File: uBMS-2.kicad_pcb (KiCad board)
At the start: 4 copper layers, 60 x 90 mm, 183 parts, among them J1 Conn_02x03_Counter_Clockwise, J2 Conn_01x02, J3 Conn_01x01, J4 Conn_01x01, J5 Conn_02x07_Odd_Even, J6 Conn_02x07_Odd_Even, J7 Conn_02x07_Odd_Even, J8 Conn_01x01, Q1 2N7002, Q10 FQD5N20L, Q11 FQD5N20L, Q12 FQD5N20L, Q13 FQD5N20L, Q14 FQD5N20L, Q15 FQD5N20L, Q2 2N7002, Q3 NTD5865NL, Q4 FQD5N20L, Q5 FQD5N20L, Q6 FQD5N20L, Q7 FQD5N20L, Q8 FQD5N20L, Q9 FQD5N20L, U1 LM2576HVS-5, U10 CD74HC4067SM, U11 CD74HC4067SM, U2 ADS1115IDGS, U3 TLV1117-33, U4 TL431DBZ, U5 ESP32-WROOM-32, U6 TSC2012IDT, U7 MCP23017_SS, U8 MCP23008-E_P, U9 VDMG10C0

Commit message: Everything is finally routed
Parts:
- moved D3 0.81 mm to (47.4, 87.7)
- moved R4 0.81 mm to (47.4, 86.2)
- moved TH2 0.43 mm to (53.3, 76.8)
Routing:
- net GND: track 104.2 -> 198.8 mm, vias 11 -> 39
- net /TempMultiplex/ESP_Temp: track 0.00 -> 92.7 mm, vias 0 -> 2
- net /TempMultiplex/Mosfet_Temp: track 12.5 -> 104.8 mm, vias 1 -> 5
- net /TempMultiplex/Power_Temp: track 0.00 -> 83.7 mm, vias 0 -> 3
- net /S2_V: track 0.00 -> 82.0 mm, vias 0 -> 2
- net /S3_V: track 0.00 -> 81.1 mm, vias 0 -> 2
- net /PrgmNode: track 0.00 -> 81.1 mm, vias 0 -> 5
- net /BTN_2: track 10.5 -> 88.0 mm, vias 1 -> 3
- net +3V3: track 163.0 -> 237.8 mm, vias 6 -> 13
- net +5V: track 76.3 -> 144.7 mm, vias 6 -> 10
- net /BTN_1: track 6.19 -> 65.1 mm, vias 1 -> 3
- net /EN: track 8.77 -> 57.0 mm, vias 0 -> 1
- net /GPIO0: track 6.69 -> 48.7 mm, vias 0 -> 3
- net /TempMultiplex/Balance_Temp: track 0.00 -> 26.4 mm, vias 0 -> 4
- net Net-(D2-Pad1): track 5.71 -> 29.5 mm, vias 0 -> 4
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- added copper zone on In2.Cu, net +5V
- added copper zone on B.Cu, net GND
- added copper zone on In1.Cu, net GND

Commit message: Fixed connections
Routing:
- net +5V: track 144.7 -> 166.4 mm, vias 10 -> 15
- net GND: track 198.8 -> 219.0 mm
- net Net-(Q3-Pad1): track 0.00 -> 2.94 mm, vias 0 -> 1
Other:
- rule trace_min: 0.2 -> 0.09
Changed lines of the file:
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@@
     (thickness 1.6)
     (drawings 8)
-    (tracks 1995)
+    (tracks 2030)
     (zones 0)
     (modules 183)
@@
   )
   (setup
-    (last_trace_width 0.2)
+    (last_trace_width 0.25)
     (user_trace_width 0.2)
     (user_trace_width 0.5)
@@
     (zone_clearance 0.508)
     (zone_45_only no)
-    (trace_min 0.2)
+    (trace_min 0.09)
     (via_size 0.8)
     (via_drill 0.4)
@@
   (via (at 75.75 56.5) (size 0.8) (drill 0.4) (layers F.Cu B.Cu) (net 1))
   (via (at 74.75 56.5) (size 0.8) (drill 0.4) (layers F.Cu B.Cu) (net 1))
-  (via (at 77.75 56.5) (size 0.8) (drill 0.4) (layers F.Cu B.Cu) (net 1))
-  (via (at 78.75 56.5) (size 0.8) (drill 0.4) (layers F.Cu B.Cu) (net 1))
+  (segment (start 27.1 36.9) (end 27.2 36.8) (width 0.5) (layer B.Cu) (net 1))
+  (segment (start 27.1 39.025) (end 27.1 36.9) (width 0.5) (layer B.Cu) (net 1))
+  (segment (start 27.2 34.55) (end 27.55 34.2) (width 0.5) (layer B.Cu) (net 1))
+  (segment (start 27.2 36.8) (end 27.2 34.55) (width 0.5) (layer B.Cu) (net 1))
+  (via (at 28.5 36.75) (size 0.8) (drill 0.4) (layers F.Cu B.Cu) (net 1))
+  (segment (start 27.2 36.8) (end 28.45 36.8) (width 0.5) (layer B.Cu) (net 1))
+  (segment (start 28.45 36.8) (end 28.5 36.75) (width 0.5) (layer B.Cu) (net 1))
+  (segment (start 40.234315 60.2) (end 40.8 60.2) (width 0.5) (layer B.Cu) (net 1))
+  (segment (start 36 60.2) (end 40.234315 60.2) (width 0.5) (layer B.Cu) (net 1))
+  (segment (start 34.375 61.825) (end 36 60.2) (width 0.5) (layer B.Cu) (net 1))
+  (segment (start 33.65 61.825) (end 34.375 61.825) (width 0.5) (layer B.Cu) (net 1))
+  (segment (start 23.6 66.8) (end 23.849999 66.8) (width 0.5) (layer F.Cu) (net 1))
+  (via (at 27.75 63.25) (size 0.8) (drill 0.4) (layers F.Cu B.Cu) (net 1))
+  (segment (start 27.75 63.525) (end 27.75 63.25) (width 0.5) (layer F.Cu) (net 1))
+  (segment (start 23.6 66.8) (end 24.475 66.8) (width 0.5) (layer F.Cu) (net 1))
+  (segment (start 24.475 66.8) (end 27.75 63.525) (width 0.5) (layer F.Cu) (net 1))
   (segment (start 30.15429 66.94429) (end 30.31 67.1) (width 0.25) (layer B.Cu) (net 2))
   (segment (start 30.85 61.825) (end 30.15429 62.52071) (width 0.25) (layer B.Cu) (net 2))
@@
   (segment (start 42.980187 36.980187) (end 41.489949 35.489949) (width 0.5) (layer B.Cu) (net 8))
   (segment (start 42.980187 37.128213) (end 42.980187 36.980187) (width 0.5) (layer B.Cu) (net 8))
-  (segment (start 27.25 45.025) (end 26.125 45.025) (width 0.25) (layer B.Cu) (net 8))
-  (segment (start 27.325001 44.949999) (end 27.25 45.025) (width 0.25) (layer B.Cu) (net 8))
-  (segment (start 26.485002 40.45) (end 27.325001 41.289999) (width 0.25) (layer B.Cu) (net 8))
-  (segment (start 23.625 40.45) (end 26.485002 40.45) (width 0.25) (layer B.Cu) (net 8))
   (segment (start 71.6 33.4) (end 70.15 34.85) (width 0.25) (layer B.Cu) (net 8))
   (segment (start 72.325 33.4) (end 71.6 33.4) (width 0.25) (layer B.Cu) (net 8))
@@
   (segment (start 54.815002 76.775) (end 56.7 74.890002) (width 0.2) (layer F.Cu) (net 8))
   (segment (start 53.595 76.775) (end 54.815002 76.775) (width 0.2) (layer F.Cu) (net 8))
-  (segment (start 27.325001 44.949999) (end 27.850001 44.949999) (width 0.2) (layer B.Cu) (net 8))
-  (segment (start 27.850001 44.949999) (end 28.9 43.9) (width 0.2) (layer B.Cu) (net 8))
-  (segment (start 28.9 42.864998) (end 27.325001 41.289999) (width 0.2) (layer B.Cu) (net 8))
-  (segment (start 28.9 43.9) (end 28.9 42.864998) (width 0.2) (layer B.Cu) (net 8))
   (segment (start 38.999999 37.000001) (end 38.6 37.4) (width 0.2) (layer B.Cu) (net 8))
   (segment (start 38.999999 35.963997) (end 38.999999 37.000001) (width 0.2) (layer B.Cu) (net 8))
@@
   (segment (start 34.117501 45.117501) (end 35.217501 44.017501) (width 1) (layer F.Cu) (net 8))
   (segment (start 35.217501 44.017501) (end 36.599999 42.635003) (width 1) (layer F.Cu) (net 8))
+  (segment (start 27.25 45.025) (end 26.125 45.025) (width 0.25) (layer B.Cu) (net 8))
+  (segment (start 27.448002 45.025) (end 27.25 45.025) (width 0.25) (layer B.Cu) (net 8))
+  (segment (start 28.525001 43.948001) (end 27.448002 45.025) (width 0.25) (layer B.Cu) (net 8))
+  (segment (start 28.525001 42.489999) (end 28.525001 43.948001) (width 0.25) (layer B.Cu) (net 8))
+  (segment (start 26.485002 40.45) (end 28.525001 42.489999) (width 0.25) (layer B.Cu) (net 8))
+  (segment (start 23.625 40.45) (end 26.485002 40.45) (width 0.25) (layer B.Cu) (net 8))
+  (segment (start 23.6 29.765685) (end 23.6 29.2) (width 0.5) (layer F.Cu) (net 8))
+  (segment (start 25.55 41.675) (end 23.6 39.725) (width 0.5) (layer F.Cu) (net 8))
+  (segment (start 25.55 44.475) (end 25.55 41.675) (width 0.5) (layer F.Cu) (net 8))
+  (via (at 22.8 30.7) (size 0.8) (drill 0.4) (layers F.Cu B.Cu) (net 8))
+  (segment (start 23.6 30.7) (end 22.8 30.7) (width 0.5) (layer F.Cu) (net 8))
+  (segment (start 23.6 30.7) (end 23.6 29.765685) (width 0.5) (layer F.Cu) (net 8))
+  (via (at 22.8 32.1) (size 0.8) (drill 0.4) (layers F.Cu B.Cu) (net 8))
+  (segment (start 23.6 32.1) (end 22.8 32.1) (width 0.5) (layer F.Cu) (net 8))
+  (segment (start 23.6 32.1) (end 23.6 30.7) (width 0.5) (layer F.Cu) (net 8))
+  (via (at 22.8 33.7) (size 0.8) (drill 0.4) (layers F.Cu B.Cu) (net 8))
+  (segment (start 23.6 33.7) (end 22.8 33.7) (width 0.5) (layer F.Cu) (net 8))
+  (segment (start 23.6 33.7) (end 23.6 32.1) (width 0.5) (layer F.Cu) (net 8))
+  (via (at 22.8 35) (size 0.8) (drill 0.4) (layers F.Cu B.Cu) (net 8))
+  (segment (start 23.6 35) (end 22.8 35) (width 0.5) (layer F.Cu) (net 8))
+  (segment (start 23.6 35) (end 23.6 33.7) (width 0.5) (layer F.Cu) (net 8))
+  (segment (start 23.6 39.725) (end 23.6 35) (width 0.5) (layer F.Cu) (net 8))
+  (via (at 70.7 31.2) (size 0.8) (drill 0.4) (layers F.Cu B.Cu) (net 8))
+  (segment (start 72.325 33.4) (end 72.325 32.825) (width 0.5) (layer B.Cu) (net 8))
+  (segment (start 72.325 32.825) (end 70.7 31.2) (width 0.5) (layer B.Cu) (net 8))
   (via (at 36.125 31.825) (size 0.8) (drill 0.4) (layers F.Cu B.Cu) (net 9))
   (segment (start 33.85 31.9) (end 36.25 31.9) (width 1) (layer B.Cu) (net 9))
@@
   (segment (start 30.375 84.035) (end 30.31 84.1) (width 0.2) (layer B.Cu) (net 91))
   (segment (start 30.375 81.325) (end 30.375 84.035) (width 0.2) (layer B.Cu) (net 91))
+  (via (at 59 22.8) (size 0.8) (drill 0.4) (layers F.Cu B.Cu) (net 92))
+  (segment (start 57.55 22.75) (end 58.95 22.75) (width 0.25) (layer B.Cu) (net 92))
+  (segment (start 58.95 22.75) (end 59 22.8) (width 0.25) (layer B.Cu) (net 92))
+  (segment (start 59 22.8) (end 57.53 22.8) (width 0.25) (layer F.Cu) (net 92))
   (segment (start 42.778858 42.564645) (end 41.435355 41.221142) (width 0.25) (layer B.Cu) (net 93))
   (segment (start 41.208578 41.221142) (end 39.868718 39.881282) (width 0.25) (layer B.Cu) (net 93))

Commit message: Added Name and Logo
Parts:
- added G***: LOGO, uBMS-2:authorFP, B.Cu at (50.5, 54.8)
- added G***: LOGO, uBMS-2:logoFP, F.Cu at (51.5, 36.0)
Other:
- board text added: "+"
- board text added: "-"
- board text added: "1"
- board text added: "10"
- board text added: "11"
- board text added: "12"
- board text added: "2"
- board text added: "3"
- board text added: "3.3"
- board text added: "4"
- board text added: "5"
- board text added: "6"
- board text added: "7"
- board text added: "8"
- board text added: "9"
- board text added: "ADC"
- board text added: "BAT"
- board text added: "Balance"
- board text added: "Current Sense"
- board text added: "EN"
- board text added: "ESP32"
- board text added: "GND"
- board text added: "PGRM"
- board text added: "Status"
- board text added: "Temp Mux"
- board text added: "Temp Sense"
- board text added: "Voltage Mux"
- board text added: "Voltage Sense"

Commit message: Generated Gerbers for JLCPCB
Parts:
- turned G*** to 180 degrees
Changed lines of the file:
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@@
     (visible_elements 7FFF7BFF)
     (pcbplotparams
-      (layerselection 0x010fc_ffffffff)
+      (layerselection 0x010f0_ffffffff)
       (usegerberextensions false)
       (usegerberattributes false)
@@
       (psa4output false)
       (plotreference true)
-      (plotvalue true)
+      (plotvalue false)
       (plotinvisibletext false)
-      (padsonsilk false)
+      (padsonsilk true)
       (subtractmaskfromsilk false)
       (outputformat 1)
       (mirror false)
-      (drillshape 1)
+      (drillshape 0)
       (scaleselection 1)
-      (outputdirectory ""))
+      (outputdirectory "gerber/"))
   )
   (net 0 "")
@@
   )
   (module uBMS-2:authorFP (layer B.Cu)
-    (at 50.5 54.75)
+    (at 50.5 54.75 180)
     (fp_text reference G*** (at 0 0) (layer B.SilkS) hide
       (effects (font (size 1.524 1.524) (thickness 0.3)) (justify mirror))

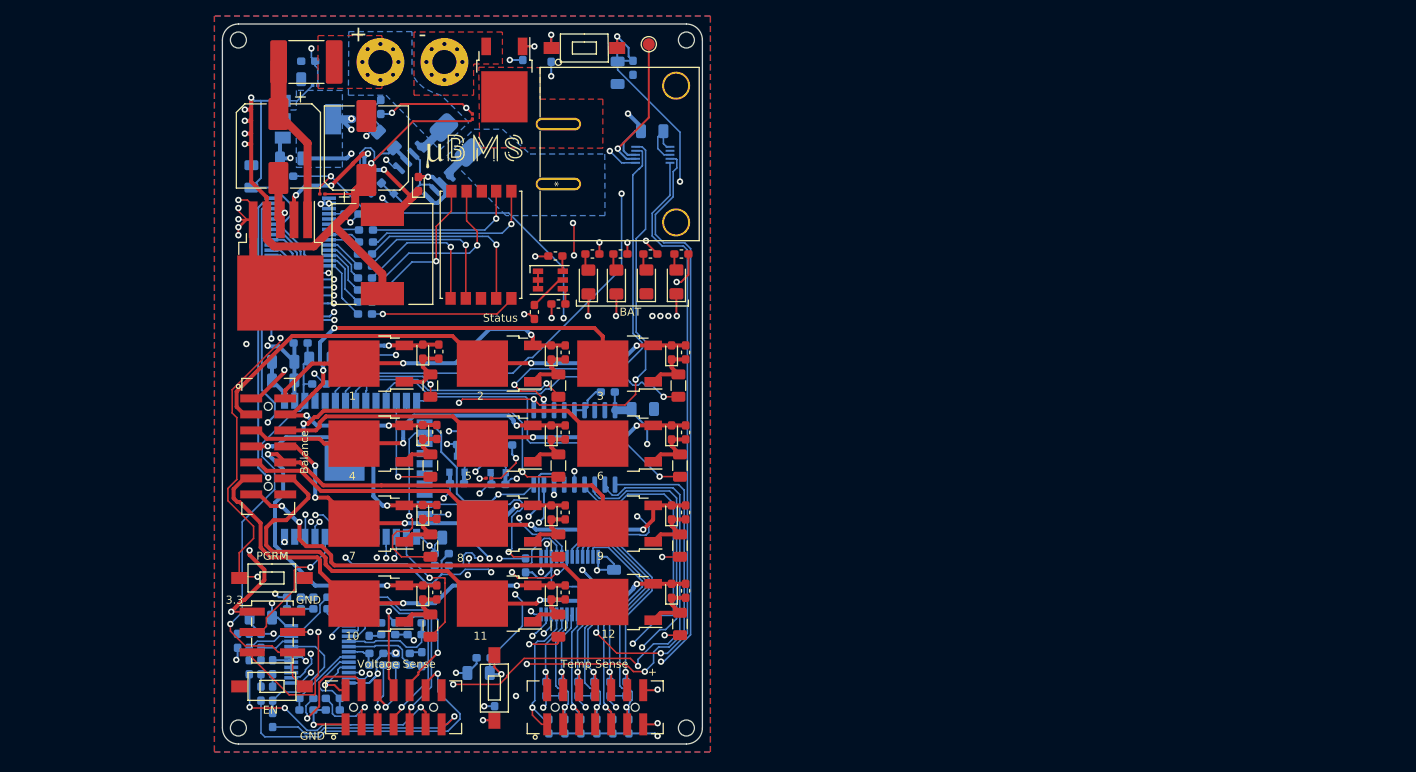
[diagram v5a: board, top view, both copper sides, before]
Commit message: Replaced GPIO expanders with shift regs
- Freed up unnessecary pins from the ESP by removing old UART signals
- Started PCB layout
- Replaced level shifter with fet arrat
- Level shifter for shift reg inputs
- Added more bat indicator LEDs
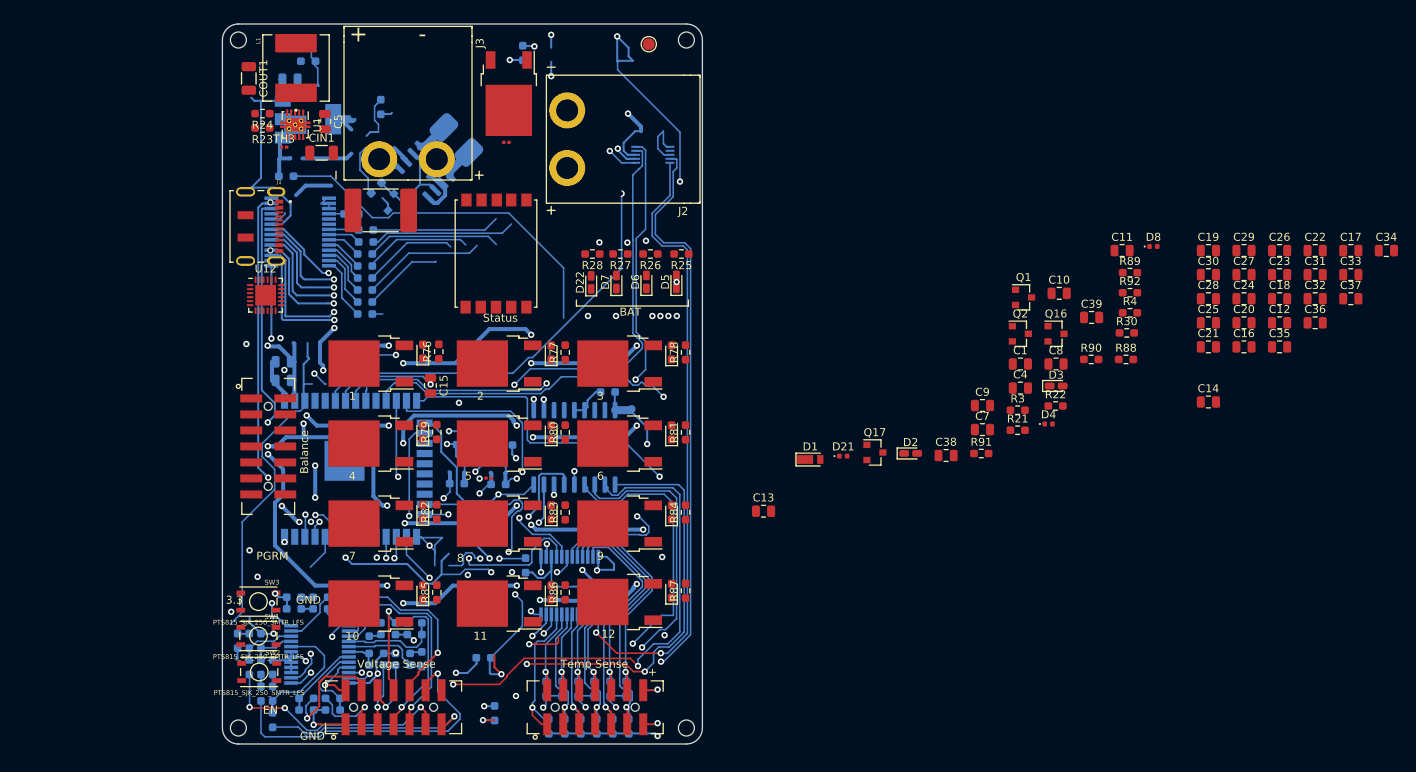
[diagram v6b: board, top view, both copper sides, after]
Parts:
- removed BTN1: Reset, Button_Switch_SMD:PTS636_SM43_SMTR_LFS_6mm_3,5mm
- removed BTN2: Program, Button_Switch_SMD:PTS636_SM43_SMTR_LFS_6mm_3,5mm
- removed BTN3: Input_1, Button_Switch_SMD:PTS636_SM43_SMTR_LFS_6mm_3,5mm
- removed BTN4: Input_2, Button_Switch_SMD:PTS636_SM43_SMTR_LFS_6mm_3,5mm
- removed G***: LOGO, uBMS-2:authorFP
- removed G***: LOGO, uBMS-2:logoFP
- removed J8: Conn_01x01, MountingHole:MountingHole_3mm_Pad_Via
- added C27: 10nF, Capacitor_SMD:C_0805_2012Metric, F.Cu at (147.7, 51.3)
- added C28: 10nF, Capacitor_SMD:C_0805_2012Metric, F.Cu at (143.2, 54.3)
- added C29: 10nF, Capacitor_SMD:C_0805_2012Metric, F.Cu at (147.7, 48.3)
- added C30: 10nF, Capacitor_SMD:C_0805_2012Metric, F.Cu at (143.2, 51.3)
- added C31: 10nF, Capacitor_SMD:C_0805_2012Metric, F.Cu at (156.6, 51.3)
- added C32: 10nF, Capacitor_SMD:C_0805_2012Metric, F.Cu at (156.6, 54.3)
- added C33: 10nF, Capacitor_SMD:C_0805_2012Metric, F.Cu at (161.1, 51.3)
- added C34: 10nF, Capacitor_SMD:C_0805_2012Metric, F.Cu at (165.5, 48.3)
- added C35: 10nF, Capacitor_SMD:C_0805_2012Metric, F.Cu at (152.2, 60.4)
- added C36: 10nF, Capacitor_SMD:C_0805_2012Metric, F.Cu at (156.6, 57.4)
- added C37: 10nF, Capacitor_SMD:C_0805_2012Metric, F.Cu at (161.1, 54.3)
- added C38: 0.1uF, Capacitor_SMD:C_0805_2012Metric, F.Cu at (110.5, 73.9)
- added C39: 0.1uF, Capacitor_SMD:C_0805_2012Metric, F.Cu at (128.7, 56.7)
- added D21: TPD1E10B06QDPYRQ1, Diode_SMD:D_0402_1005Metric, F.Cu at (97.6, 74.0)
- added D22: GREEN_LED, LED_SMD:LED_0603_1608Metric_Castellated, F.Cu at (66.1, 52.3)
- added Q16: 2N7002, Package_TO_SOT_SMD:SOT-23, F.Cu at (124.2, 58.7)
- added Q17: 2N7002, Package_TO_SOT_SMD:SOT-23, F.Cu at (101.6, 73.6)
- added R88: 5.1k, Resistor_SMD:R_0603_1608Metric_Pad0.98x0.95mm_HandSolder, F.Cu at (132.9, 61.9)
- added R89: 47R, Resistor_SMD:R_0603_1608Metric_Pad0.98x0.95mm_HandSolder, F.Cu at (133.4, 51.1)
- added R90: 10k, Resistor_SMD:R_0603_1608Metric_Pad0.98x0.95mm_HandSolder, F.Cu at (128.6, 61.9)
- added R91: 47R, Resistor_SMD:R_0603_1608Metric_Pad0.98x0.95mm_HandSolder, F.Cu at (114.9, 73.7)
- added R92: 10k, Resistor_SMD:R_0603_1608Metric_Pad0.98x0.95mm_HandSolder, F.Cu at (133.4, 53.6)
- added SW1: PTS815_SJK_250_SMTR_LFS, ClementsFootprints:PTS815_SJK_250_SMTR_LFS, F.Cu at (24.5, 96.5)
- added SW2: PTS815_SJK_250_SMTR_LFS, ClementsFootprints:PTS815_SJK_250_SMTR_LFS, F.Cu at (24.6, 101.0)
- added SW3: PTS815_SJK_250_SMTR_LFS, ClementsFootprints:PTS815_SJK_250_SMTR_LFS, F.Cu at (24.5, 92.2)
- added U12: CP2102N-A02-GQFN24, Package_DFN_QFN:QFN-24-1EP_4x4mm_P0.5mm_EP2.6x2.6mm, F.Cu at (25.4, 53.9)
- C1, C10, C11, C13, C14, C4, C9: footprint Capacitor_SMD:C_1206_3216Metric -> Capacitor_SMD:C_0805_2012Metric; moved to F.Cu
- C12: value 0.1uF -> 10nF; footprint Capacitor_SMD:C_1206_3216Metric -> Capacitor_SMD:C_0805_2012Metric; moved to F.Cu
- C15, C16, C17, C18, C19, C2, C20, C21, C22, C23, C24, C25, C26, C3, C6: footprint Capacitor_SMD:C_1206_3216Metric -> Capacitor_SMD:C_0805_2012Metric
- C5: value 2.2uF -> 33nF; footprint Capacitor_SMD:C_1206_3216Metric -> Capacitor_SMD:C_0805_2012Metric; moved to F.Cu
- C7: value 1uF -> 0.1uF; footprint Capacitor_SMD:C_1206_3216Metric -> Capacitor_SMD:C_0805_2012Metric; moved to F.Cu
- C8: value 0.1uF -> 1uF; footprint Capacitor_SMD:C_1206_3216Metric -> Capacitor_SMD:C_0805_2012Metric; moved to F.Cu
- CIN1: value 100uF 60V -> 2.2uF; footprint Capacitor_SMD:CP_Elec_10x10 -> Capacitor_SMD:C_1206_3216Metric
- COUT1: value 1000uF -> 47uF; footprint Capacitor_SMD:CP_Elec_10x10 -> Capacitor_SMD:C_1206_3216Metric
- D1: value D -> RB162VAM-20TR; footprint Diode_SMD:D_0603_1608Metric_Pad1.05x0.95mm_HandSolder -> Diode_SMD:D_TUMD2; moved to F.Cu
- D2: value D -> 150060VS55040; footprint Diode_SMD:D_0603_1608Metric_Pad1.05x0.95mm_HandSolder -> LED_SMD:LED_0603_1608Metric_Castellated
- D3: value D -> 150060SS55040; footprint Diode_SMD:D_0603_1608Metric_Pad1.05x0.95mm_HandSolder -> LED_SMD:LED_0603_1608Metric_Castellated; moved to F.Cu
- D4: value CLX6F-FKC -> TPD1E10B06QDPYRQ1; footprint LED_SMD:LED_RGB_PLCC-6 -> Diode_SMD:D_0402_1005Metric
- D5: value LED -> RED_LED; footprint LED_SMD:LED_1206_3216Metric_Pad1.42x1.75mm_HandSolder -> LED_SMD:LED_0603_1608Metric_Castellated
- D6: value LED -> YELLOW_LED; footprint LED_SMD:LED_1206_3216Metric_Pad1.42x1.75mm_HandSolder -> LED_SMD:LED_0603_1608Metric_Castellated
- D7: value LED -> GREEN_LED; footprint LED_SMD:LED_1206_3216Metric_Pad1.42x1.75mm_HandSolder -> LED_SMD:LED_0603_1608Metric_Castellated
- D8: value LED -> TPD1E10B06QDPYRQ1; footprint LED_SMD:LED_1206_3216Metric_Pad1.42x1.75mm_HandSolder -> Diode_SMD:D_0402_1005Metric
- F1: value 1A PTC -> 0ZCF0030FF2C
- J1: value Conn_02x03_Counter_Clockwise -> DX07S016JA1R1500; footprint Connector_PinHeader_2.54mm:PinHeader_2x03_P2.54mm_Vertical_SMD -> ClementsFootprints:DX07S016JA1R1500
- J2: value Conn_01x02 -> XT60PW-M20; footprint uBMS-2:1720430202 -> ClementsFootprints:XT60PW-M20
- J3: value Conn_01x01 -> XT60PW-M20; footprint MountingHole:MountingHole_3mm_Pad_Via -> ClementsFootprints:XT60PW-M20
- L1: footprint Inductor_SMD:L_12x12mm_H8mm -> ClementsFootprints:1267AY-101M=P3
- Q1, Q2: moved to F.Cu
- R1, R10, R11, R12, R13, R14, R15, R16, R17, R18, R19, R2, R20, R29, R31, R32, R33, R34, R35, R36, R37, R38, R39, R40, R41, R42, R43, R44, R45, R46, R47, R48, R49, R5, R50, R51, R52, R53, R54, R55, R56, R57, R58, R59, R6, R60, R61, R62, R63, R64, R65, R66, R67, R68, R69, R70, R71, R72, R73, R74, R75, R76, R77, R78, R79, R8, R80, R81, R82, R83, R84, R85, R86, R87, R9: footprint Resistor_SMD:R_0603_1608Metric_Pad1.05x0.95mm_HandSolder -> Resistor_SMD:R_0603_1608Metric_Pad0.98x0.95mm_HandSolder
- R21: value 4.7k -> 10k; footprint Resistor_SMD:R_0603_1608Metric_Pad1.05x0.95mm_HandSolder -> Resistor_SMD:R_0603_1608Metric_Pad0.98x0.95mm_HandSolder; moved to F.Cu
- R22: value 270R -> 10k; footprint Resistor_SMD:R_0603_1608Metric_Pad1.05x0.95mm_HandSolder -> Resistor_SMD:R_0603_1608Metric_Pad0.98x0.95mm_HandSolder
- R23: value 270R -> 71.5k; footprint Resistor_SMD:R_0603_1608Metric_Pad1.05x0.95mm_HandSolder -> Resistor_SMD:R_0603_1608Metric_Pad0.98x0.95mm_HandSolder
- R24: value 270R -> 105k; footprint Resistor_SMD:R_0603_1608Metric_Pad1.05x0.95mm_HandSolder -> Resistor_SMD:R_0603_1608Metric_Pad0.98x0.95mm_HandSolder
- R25, R26, R27, R28: value 270R -> 470R; footprint Resistor_SMD:R_0603_1608Metric_Pad1.05x0.95mm_HandSolder -> Resistor_SMD:R_0603_1608Metric_Pad0.98x0.95mm_HandSolder
- R3, R4: value 10k -> 330R; footprint Resistor_SMD:R_0603_1608Metric_Pad1.05x0.95mm_HandSolder -> Resistor_SMD:R_0603_1608Metric_Pad0.98x0.95mm_HandSolder; moved to F.Cu
- R30: value 4.7k -> 5.1k; footprint Resistor_SMD:R_0603_1608Metric_Pad1.05x0.95mm_HandSolder -> Resistor_SMD:R_0603_1608Metric_Pad0.98x0.95mm_HandSolder; moved to F.Cu
- U1: value LM2576HVS-5 -> LM5166X; footprint Package_TO_SOT_SMD:TO-263-5_TabPin3 -> Package_SON:Texas_S-PVSON-N10_ThermalVias
- moved C24 109.6 mm to (147.7, 54.3), turned to 0 degrees
- moved C18 108.2 mm to (152.2, 54.3), turned to 0 degrees
- moved C22 101.5 mm to (156.6, 48.3), turned to 0 degrees
- moved C21 100.4 mm to (143.2, 60.4), turned to 0 degrees
- moved C11 96.2 mm to (132.5, 48.3), turned to 0 degrees
- moved C9 95.8 mm to (115.0, 67.7), turned to 0 degrees
- moved C7 92.8 mm to (115.0, 70.7), turned to 0 degrees
- moved R4 91.1 mm to (133.4, 56.1), turned to 0 degrees
- moved R3 90.0 mm to (119.4, 68.3)
- moved C25 89.6 mm to (143.2, 57.4), turned to 0 degrees
- moved C12 88.5 mm to (152.2, 57.4), turned to 0 degrees
- moved C26 88.3 mm to (152.2, 48.3), turned to 0 degrees
- moved C8 88.3 mm to (124.2, 62.5), turned to 0 degrees
- moved C4 87.6 mm to (119.8, 65.5)
- moved C16 85.8 mm to (147.7, 60.4), turned to 0 degrees
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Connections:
- C11 pad 1: /BTN_1 -> +5V
- C12 pad 1: /BTN_2 -> /BatteryBalance/Cell1_P
- C16 pad 2: /PWM_Blnce_2 -> /PWM_Blnce_5
- C17 pad 2: /PWM_Blnce_3 -> /PWM_Blnce_9
- C18 pad 1: Net-(C18-Pad1) -> /BatteryBalance/Cell5_P
- C18 pad 2: /PWM_Blnce_4 -> /BatteryBalance/Cell4_P
- C19 pad 1: Net-(C19-Pad1) -> /BatteryBalance/Cell9_P
- C19 pad 2: /PWM_Blnce_5 -> /BatteryBalance/Cell8_P
- C20 pad 2: /PWM_Blnce_6 -> /PWM_Blnce_2
- C21 pad 2: /PWM_Blnce_7 -> /PWM_Blnce_6
- C22 pad 2: /PWM_Blnce_8 -> /PWM_Blnce_10
- C23 pad 1: Net-(C23-Pad1) -> /BatteryBalance/Cell2_P
- C23 pad 2: /PWM_Blnce_9 -> /BatteryBalance/Cell1_P
- C24 pad 1: Net-(C24-Pad1) -> /BatteryBalance/Cell6_P
- C24 pad 2: /PWM_Blnce_10 -> /BatteryBalance/Cell5_P
- C25 pad 1: Net-(C25-Pad1) -> /BatteryBalance/Cell10_P
- C25 pad 2: /PWM_Blnce_11 -> /BatteryBalance/Cell9_P
- C26 pad 2: /PWM_Blnce_12 -> /PWM_Blnce_3
- C4 pad 1: /EN -> /BTN_1
- C5 pad 1: /GPIO0 -> Net-(C5-Pad1)
- C7 pad 1: +3V3 -> +5V
- C8 pad 1: +5V -> +3V3
- D1 pad 1: /PrgmNode -> +5V
- D1 pad 2: /EN -> /VBUS
- D10 pad 1: Net-(C16-Pad1) -> Net-(C20-Pad1)
- D11 pad 1: Net-(C17-Pad1) -> Net-(C26-Pad1)
- D12 pad 1: Net-(C18-Pad1) -> Net-(C32-Pad1)
- D13 pad 1: Net-(C19-Pad1) -> Net-(C16-Pad1)
- D14 pad 1: Net-(C20-Pad1) -> Net-(C21-Pad1)
- D15 pad 1: Net-(C21-Pad1) -> Net-(C27-Pad1)
- D16 pad 1: Net-(C22-Pad1) -> Net-(C33-Pad1)
- D17 pad 1: Net-(C23-Pad1) -> Net-(C17-Pad1)
- D18 pad 1: Net-(C24-Pad1) -> Net-(C22-Pad1)
- D19 pad 1: Net-(C25-Pad1) -> Net-(C28-Pad1)
- D2 pad 2: GND -> Net-(D2-Pad2)
- D20 pad 1: Net-(C26-Pad1) -> Net-(C34-Pad1)
- D3 pad 1: /PrgmNode -> Net-(D3-Pad1)
- D3 pad 2: /GPIO0 -> Net-(D3-Pad2)
- D4 pad 1: GND -> /USB_D+
- D8 pad 1: GND -> /USB_D-
- D8 pad 2: Net-(D8-Pad2) -> GND
- J1 pad 1: +3V3 -> GND
- J1 pad 2: GND -> /VBUS
- J1 pad 3: /UART_RX -> Net-(J1-Pad3)
- J1 pad 4: /UART_TX -> Net-(J1-Pad4)
- J1 pad 5: /GPIO0 -> /USB_D-
- J1 pad 6: /EN -> /USB_D+
- J3 pad 1: /Batt_Pos -> GND
- L1 pad 1: Net-(D2-Pad1) -> Net-(L1-Pad1)
- Q10 pad 1: Net-(C21-Pad1) -> Net-(C27-Pad1)
- Q11 pad 1: Net-(C22-Pad1) -> Net-(C33-Pad1)
- Q12 pad 1: Net-(C23-Pad1) -> Net-(C17-Pad1)
- Q13 pad 1: Net-(C24-Pad1) -> Net-(C22-Pad1)
- Q14 pad 1: Net-(C25-Pad1) -> Net-(C28-Pad1)
- Q15 pad 1: Net-(C26-Pad1) -> Net-(C34-Pad1)
- Q5 pad 1: Net-(C16-Pad1) -> Net-(C20-Pad1)
- Q6 pad 1: Net-(C17-Pad1) -> Net-(C26-Pad1)
- Q7 pad 1: Net-(C18-Pad1) -> Net-(C32-Pad1)
- Q8 pad 1: Net-(C19-Pad1) -> Net-(C16-Pad1)
- Q9 pad 1: Net-(C20-Pad1) -> Net-(C21-Pad1)
- R21 pad 1: Net-(BTN4-Pad1) -> +5V
- R21 pad 2: +3V3 -> Net-(R21-Pad2)
- R22 pad 1: /LED_B -> GND
- R22 pad 2: Net-(D4-Pad6) -> /VBUS
- R23 pad 1: /LED_G -> Net-(R23-Pad1)
- R23 pad 2: Net-(D4-Pad5) -> GND
- R24 pad 1: /LED_R -> GND
- R24 pad 2: Net-(D4-Pad4) -> Net-(R24-Pad2)
- R28 pad 2: Net-(D8-Pad2) -> Net-(D22-Pad2)
- R3 pad 2: /EN -> Net-(D2-Pad2)
- R30 pad 2: /BTN_2 -> Net-(J1-Pad9)
- R4 pad 2: /GPIO0 -> Net-(D3-Pad2)
- R77 pad 1: Net-(C16-Pad1) -> Net-(C20-Pad1)
- R78 pad 1: Net-(C17-Pad1) -> Net-(C26-Pad1)
- R79 pad 1: Net-(C18-Pad1) -> Net-(C32-Pad1)
- R80 pad 1: Net-(C19-Pad1) -> Net-(C16-Pad1)
- R81 pad 1: Net-(C20-Pad1) -> Net-(C21-Pad1)
- R82 pad 1: Net-(C21-Pad1) -> Net-(C27-Pad1)
- R83 pad 1: Net-(C22-Pad1) -> Net-(C33-Pad1)
- R84 pad 1: Net-(C23-Pad1) -> Net-(C17-Pad1)
- R85 pad 1: Net-(C24-Pad1) -> Net-(C22-Pad1)
- R86 pad 1: Net-(C25-Pad1) -> Net-(C28-Pad1)
- R87 pad 1: Net-(C26-Pad1) -> Net-(C34-Pad1)
- U1 pad 1: Net-(CIN1-Pad1) -> Net-(L1-Pad1)
- U1 pad 2: Net-(D2-Pad1) -> Net-(CIN1-Pad1)
- U1 pad 3: GND -> Net-(R24-Pad2)
- U1 pad 4: +5V -> Net-(C5-Pad1)
- U1 pad 5: GND -> Net-(R23-Pad1)
- U5 pad 25: /GPIO0 -> /ESP_IO0
- U5 pad 29: Net-(U5-Pad29) -> /CTS
- U5 pad 3: /EN -> /ESP_EN
- U5 pad 30: Net-(U5-Pad30) -> /DSR
- U5 pad 31: Net-(U5-Pad31) -> /DCD
- U5 pad 39: (no net) -> GND
- U5 pad 7: /BTN_2 -> /USB_SUSPEND
- U7 pad 2: /LED_R -> Net-(U7-Pad2)
- U7 pad 3: /LED_G -> Net-(U7-Pad3)
- U7 pad 4: /LED_B -> Net-(U7-Pad4)
- U8 pad 18: GND -> +5V
- U8 pad 9: +5V -> GND
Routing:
- net /BTN_2: track 88.0 -> 0.00 mm, vias 3 -> 0
- net /USB_SUSPEND: track 0.00 -> 86.6 mm, vias 0 -> 3
- net +5V: track 166.4 -> 89.6 mm, vias 15 -> 8
- net /BatteryBalance/Cell11_P: track 70.6 -> 13.1 mm
- net /EN: track 57.0 -> 0.00 mm, vias 1 -> 0
- net GND: track 219.0 -> 163.6 mm, vias 39 -> 26
- net /BatteryBalance/Cell3_P: track 71.1 -> 17.0 mm
- net /BatteryBalance/Cell9_P: track 82.4 -> 28.7 mm
- net /BatteryBalance/Cell2_P: track 65.5 -> 14.1 mm
- net /GPIO0: track 48.7 -> 0.00 mm, vias 3 -> 0
- net /BatteryBalance/Cell12_P: track 51.3 -> 3.03 mm
- net /BatteryBalance/Cell6_P: track 72.7 -> 24.6 mm
- net /BatteryBalance/Cell8_P: track 60.1 -> 14.2 mm
- net /LED_R: track 44.1 -> 0.00 mm, vias 2 -> 0
- net /LED_B: track 42.4 -> 0.00 mm, vias 2 -> 0
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- removed copper zone on B.Cu, net +3V3
- removed copper zone on In2.Cu, net +5V
- removed copper zone on B.Cu, net /Batt_Pos
- removed copper zone on F.Cu, net /Batt_Pos
- removed copper zone on B.Cu, net /SYS_Pos
- removed copper zone on F.Cu, net /SYS_RTN
- removed copper zone on B.Cu, net GND
- removed copper zone on F.Cu, net GND
- removed copper zone on In1.Cu, net GND
